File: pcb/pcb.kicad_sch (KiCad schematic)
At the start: 7 parts

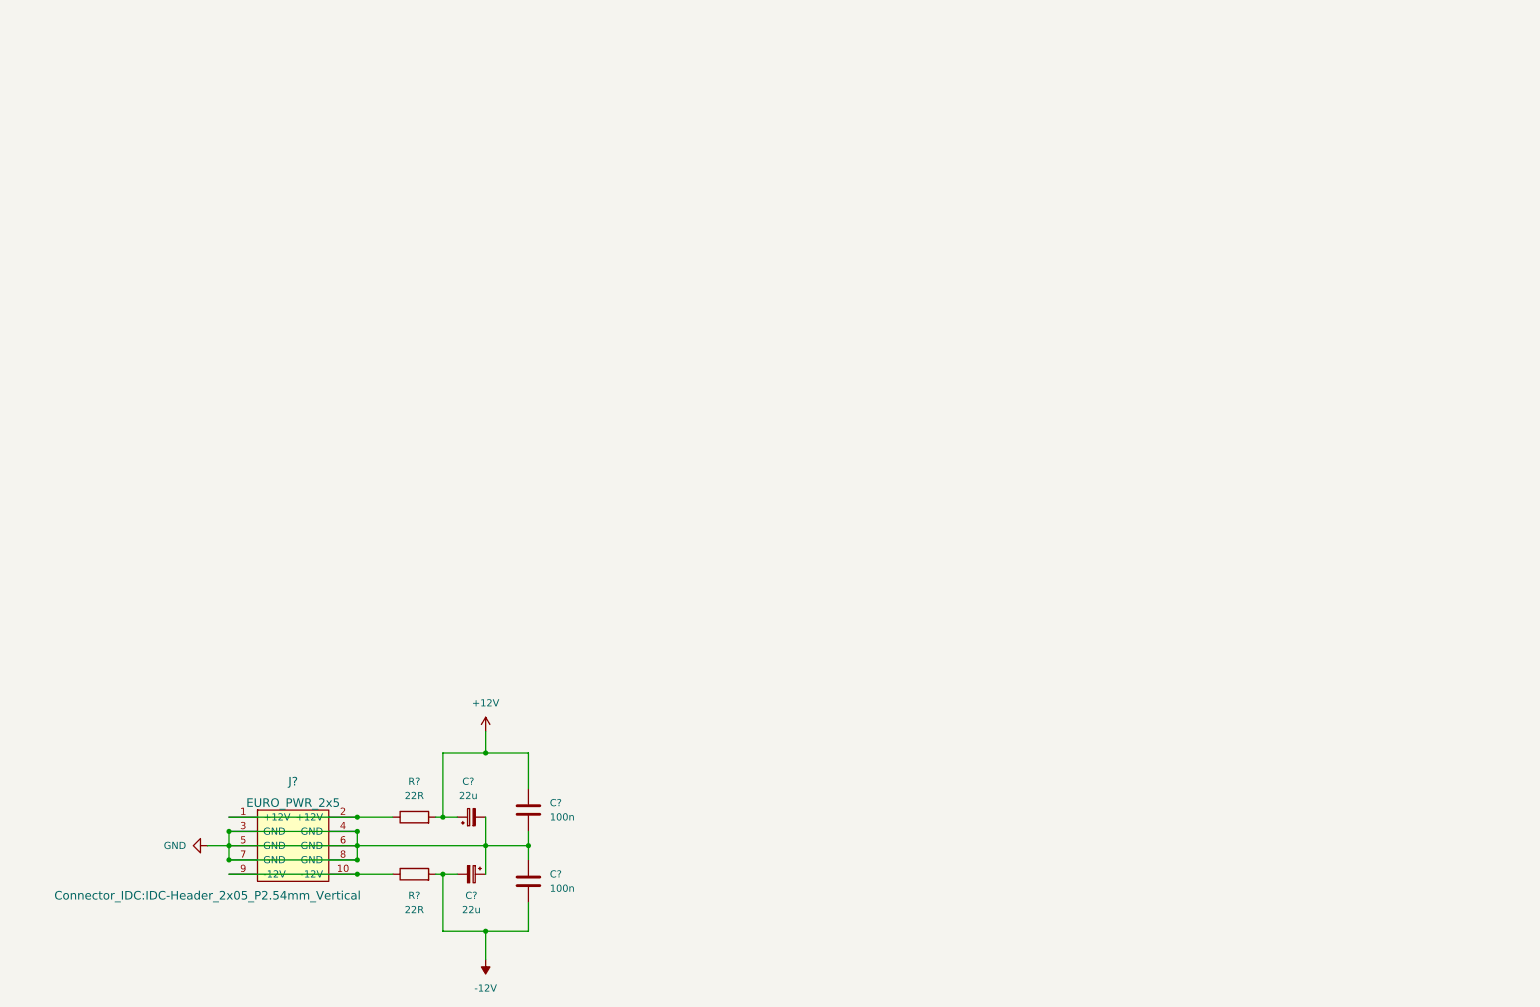
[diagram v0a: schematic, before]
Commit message: Add schematic, first panel design
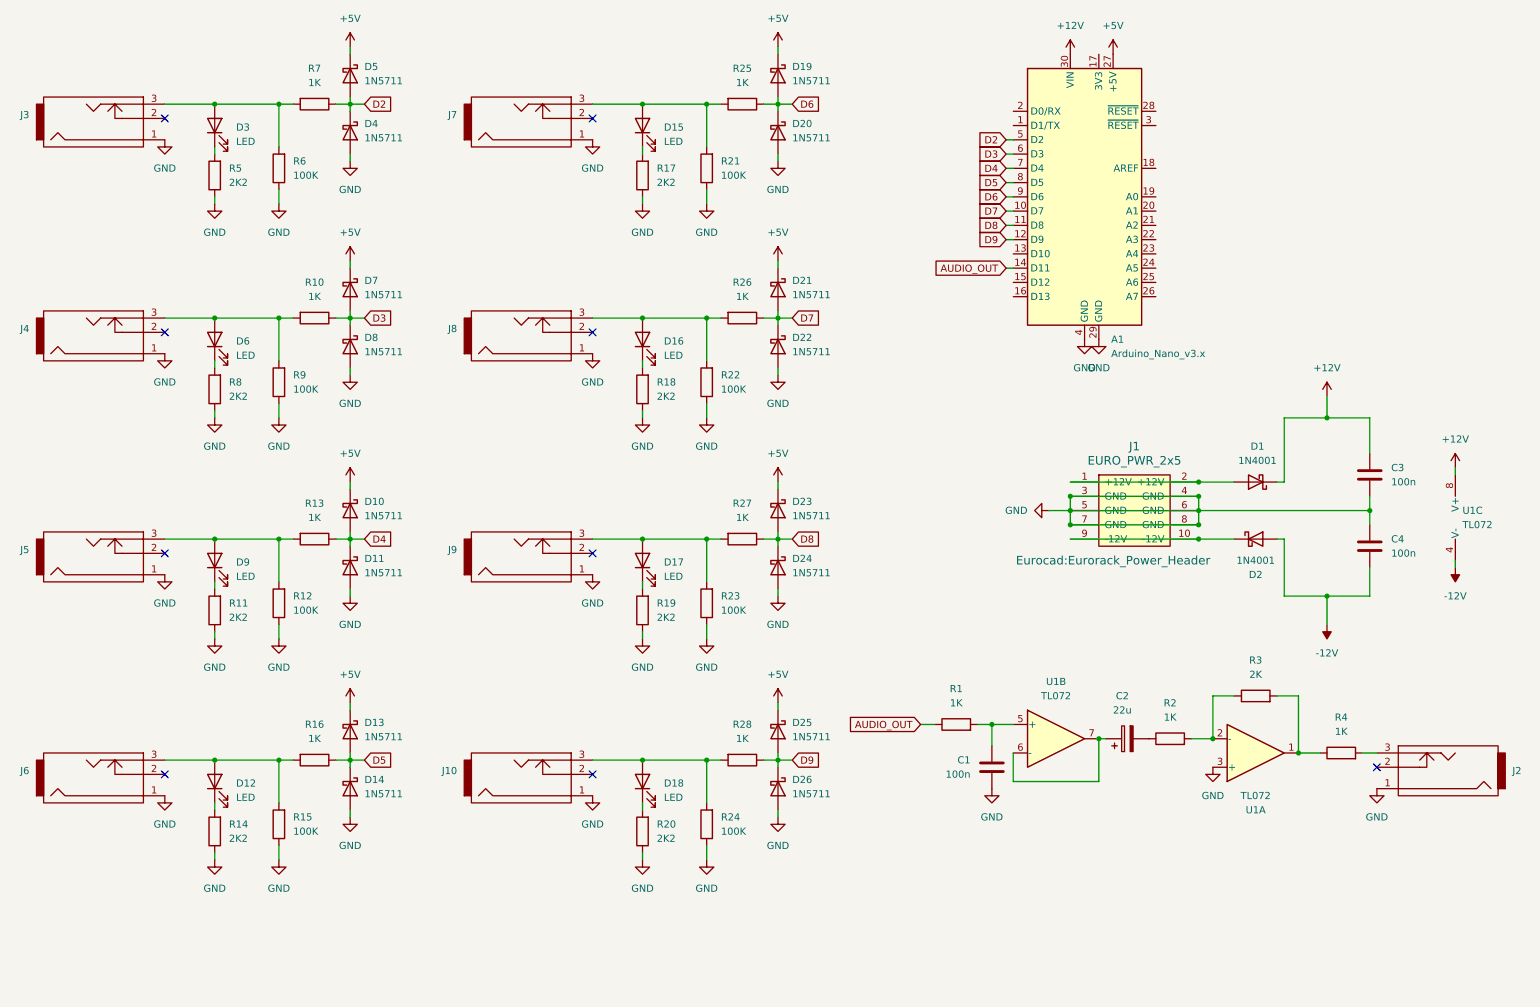
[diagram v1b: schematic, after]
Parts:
- removed C? (x2): 100n, Capacitor_SMD:C_0603_1608Metric, symbol Device:C
- removed C? (x2): 22u, Capacitor_SMD:CP_Elec_4x3.9, symbol Device:C_Polarized_Small
- removed J?: EURO_PWR_2x5, Connector_IDC:IDC-Header_2x05_P2.54mm_Vertical, symbol eurocad:EURO_PWR_2x5
- removed R? (x2): 22R, Resistor_SMD:R_0603_1608Metric, symbol Device:R
- added A1: Arduino_Nano_v3.x, Module:Arduino_Nano, symbol MCU_Module:Arduino_Nano_v3.x
- added C1, C3, C4: 100n, Capacitor_THT:C_Rect_L7.2mm_W3.0mm_P5.00mm_FKS2_FKP2_MKS2_MKP2, symbol Device:C
- added C2: 22u, Capacitor_THT:CP_Radial_D5.0mm_P2.50mm, symbol Device:C_Polarized
- added D1, D2: 1N4001, Diode_THT:D_DO-41_SOD81_P10.16mm_Horizontal, symbol Diode:1N5819
- added D10, D11, D13, D14, D19, D20, D21, D22, D23, D24, D25, D26, D4, D5, D7, D8: 1N5711, Diode_THT:D_DO-41_SOD81_P10.16mm_Horizontal, symbol Diode:1N5819
- added D12, D15, D16, D17, D18, D3, D6, D9: LED, LED_THT:LED_D3.0mm, symbol Device:LED
- added J1: EURO_PWR_2x5, Eurocad:Eurorack_Power_Header, symbol eurocad:EURO_PWR_2x5
- added J10, J2, J3, J4, J5, J6, J7, J8, J9: PJ301M-12, Eurocad:PJ301M-12, symbol eurocad:PJ301M-12
- added R1, R10, R13, R16, R2, R25, R26, R27, R28, R4, R7: 1K, Resistor_THT:R_Axial_DIN0207_L6.3mm_D2.5mm_P7.62mm_Horizontal, symbol Device:R
- added R11, R14, R17, R18, R19, R20, R5, R8: 2K2, Resistor_THT:R_Axial_DIN0207_L6.3mm_D2.5mm_P7.62mm_Horizontal, symbol Device:R
- added R12, R15, R21, R22, R23, R24, R6, R9: 100K, Resistor_THT:R_Axial_DIN0207_L6.3mm_D2.5mm_P7.62mm_Horizontal, symbol Device:R
- added R3: 2K, Resistor_THT:R_Axial_DIN0207_L6.3mm_D2.5mm_P7.62mm_Horizontal, symbol Device:R
- added U1: TL072, symbol Amplifier_Operational:TL072
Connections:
- net +12V: now also A1.30 (VIN), C3.1, D1.1 (K), U1.8 (V+)
- net -12V: now also C4.2, D2.2 (A), U1.4 (V-)
- net GND: now also A1.29 (GND), A1.4 (GND), C1.2, C3.2, C4.1, D11.2 (A), D14.2 (A), D20.2 (A), D22.2 (A), D24.2 (A), D26.2 (A), D4.2 (A), D8.2 (A), J1.3 (GND), J1.4 (GND), J1.5 (GND), J1.6 (GND), J1.7 (GND), J1.8 (GND), J10.1, J2.1, J3.1, J4.1, J5.1, J6.1, J7.1, J8.1, J9.1, R11.1, R12.1, R14.1, R15.1, R17.1, R18.1, R19.1, R20.1, R21.1, R22.1, R23.1, R24.1, R5.1, R6.1, R8.1, R9.1, U1.3 (+)
- new net: D12.2 (A), J6.3, R15.2, R16.2
- new net: D12.1 (K), R14.2
- new net: D18.2 (A), J10.3, R24.2, R28.2
- new net: D16.2 (A), J8.3, R22.2, R26.2
- new net: D6.2 (A), J4.3, R10.2, R9.2
- new net: D18.1 (K), R20.2
- new net: D3.1 (K), R5.2
- new net: D3.2 (A), J3.3, R6.2, R7.2
- new net: D2.1 (K), J1.10 (-12V), J1.9 (-12V)
- new net: R2.2, R3.1, U1.2 (-)
- new net: R3.2, R4.1, U1.1
- new net: C1.1, R1.2, U1.5 (+)
- new net: D9.1 (K), R11.2
- new net: D9.2 (A), J5.3, R12.2, R13.2
- new net: D17.1 (K), R19.2
- new net: D17.2 (A), J9.3, R23.2, R27.2
- new net: C2.1, U1.6 (-), U1.7
- new net: C2.2, R2.1
- new net: D15.2 (A), J7.3, R21.2, R25.2
- new net: D15.1 (K), R17.2
- new net: D6.1 (K), R8.2
- new net: J2.3, R4.2
- new net: D16.1 (K), R18.2
- new net: D1.2 (A), J1.1 (+12V), J1.2 (+12V)
- new net +5V: A1.27 (+5V), D10.1 (K), D13.1 (K), D19.1 (K), D21.1 (K), D23.1 (K), D25.1 (K), D5.1 (K), D7.1 (K)
- new net AUDIO_OUT: A1.14 (D11), R1.1
- new net D2: A1.5 (D2), D4.1 (K), D5.2 (A), R7.1
- new net D3: A1.6 (D3), D7.2 (A), D8.1 (K), R10.1
- new net D4: A1.7 (D4), D10.2 (A), D11.1 (K), R13.1
- new net D5: A1.8 (D5), D13.2 (A), D14.1 (K), R16.1
- new net D6: A1.9 (D6), D19.2 (A), D20.1 (K), R25.1
- new net D7: A1.10 (D7), D21.2 (A), D22.1 (K), R26.1
- new net D8: A1.11 (D8), D23.2 (A), D24.1 (K), R27.1
- new net D9: A1.12 (D9), D25.2 (A), D26.1 (K), R28.1
- no-connect marks 0 -> 9

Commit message: Finish pcb
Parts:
- D10, D11, D13, D14, D19, D20, D21, D22, D23, D24, D25, D26, D4, D5, D7, D8: footprint Diode_THT:D_DO-41_SOD81_P10.16mm_Horizontal -> Diode_THT:D_DO-35_SOD27_P7.62mm_Horizontal
- U1: footprint (none) -> Package_DIP:DIP-8_W7.62mm
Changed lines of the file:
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@@
       (effects (font (size 1.27 1.27)) (justify left))
     )
-    (property "Footprint" "Diode_THT:D_DO-41_SOD81_P10.16mm_Horizontal" (at 145.415 76.2 0)
+    (property "Footprint" "Diode_THT:D_DO-35_SOD27_P7.62mm_Horizontal" (at 145.415 76.2 0)
       (effects (font (size 1.27 1.27)) hide)
     )
@@
       (effects (font (size 1.27 1.27)) (justify left))
     )
-    (property "Footprint" "Diode_THT:D_DO-41_SOD81_P10.16mm_Horizontal" (at 69.215 66.04 0)
+    (property "Footprint" "Diode_THT:D_DO-35_SOD27_P7.62mm_Horizontal" (at 69.215 66.04 0)
       (effects (font (size 1.27 1.27)) hide)
     )
@@
       (effects (font (size 1.27 1.27)) (justify left))
     )
-    (property "Footprint" "Diode_THT:D_DO-41_SOD81_P10.16mm_Horizontal" (at 145.415 66.04 0)
+    (property "Footprint" "Diode_THT:D_DO-35_SOD27_P7.62mm_Horizontal" (at 145.415 66.04 0)
       (effects (font (size 1.27 1.27)) hide)
     )
@@
       (effects (font (size 1.27 1.27)) (justify left))
     )
-    (property "Footprint" "Diode_THT:D_DO-41_SOD81_P10.16mm_Horizontal" (at 69.215 154.94 0)
+    (property "Footprint" "Diode_THT:D_DO-35_SOD27_P7.62mm_Horizontal" (at 69.215 154.94 0)
       (effects (font (size 1.27 1.27)) hide)
     )
@@
       (effects (font (size 1.27 1.27)))
     )
-    (property "Footprint" "" (at 234.95 148.59 0)
+    (property "Footprint" "Package_DIP:DIP-8_W7.62mm" (at 234.95 148.59 0)
       (effects (font (size 1.27 1.27)) hide)
     )
@@
       (effects (font (size 1.27 1.27)) (justify left))
     )
-    (property "Footprint" "Diode_THT:D_DO-41_SOD81_P10.16mm_Horizontal" (at 145.415 144.78 0)
+    (property "Footprint" "Diode_THT:D_DO-35_SOD27_P7.62mm_Horizontal" (at 145.415 144.78 0)
       (effects (font (size 1.27 1.27)) hide)
     )
@@
       (effects (font (size 1.27 1.27)) (justify left))
     )
-    (property "Footprint" "Diode_THT:D_DO-41_SOD81_P10.16mm_Horizontal" (at 69.215 27.94 0)
+    (property "Footprint" "Diode_THT:D_DO-35_SOD27_P7.62mm_Horizontal" (at 69.215 27.94 0)
       (effects (font (size 1.27 1.27)) hide)
     )
@@
       (effects (font (size 1.27 1.27)) (justify left))
     )
-    (property "Footprint" "Diode_THT:D_DO-41_SOD81_P10.16mm_Horizontal" (at 145.415 38.1 0)
+    (property "Footprint" "Diode_THT:D_DO-35_SOD27_P7.62mm_Horizontal" (at 145.415 38.1 0)
       (effects (font (size 1.27 1.27)) hide)
     )
@@
       (effects (font (size 1.27 1.27)) (justify left))
     )
-    (property "Footprint" "Diode_THT:D_DO-41_SOD81_P10.16mm_Horizontal" (at 145.415 27.94 0)
+    (property "Footprint" "Diode_THT:D_DO-35_SOD27_P7.62mm_Horizontal" (at 145.415 27.94 0)
       (effects (font (size 1.27 1.27)) hide)
     )
@@
       (effects (font (size 1.27 1.27)) (justify left))
     )
-    (property "Footprint" "Diode_THT:D_DO-41_SOD81_P10.16mm_Horizontal" (at 69.215 38.1 0)
+    (property "Footprint" "Diode_THT:D_DO-35_SOD27_P7.62mm_Horizontal" (at 69.215 38.1 0)
       (effects (font (size 1.27 1.27)) hide)
     )
@@
       (effects (font (size 1.27 1.27)))
     )
-    (property "Footprint" "" (at 199.39 146.05 0)
+    (property "Footprint" "Package_DIP:DIP-8_W7.62mm" (at 199.39 146.05 0)
       (effects (font (size 1.27 1.27)) hide)
     )
@@
       (effects (font (size 1.27 1.27)) (justify left))
     )
-    (property "Footprint" "Diode_THT:D_DO-41_SOD81_P10.16mm_Horizontal" (at 69.215 115.57 0)
+    (property "Footprint" "Diode_THT:D_DO-35_SOD27_P7.62mm_Horizontal" (at 69.215 115.57 0)
       (effects (font (size 1.27 1.27)) hide)
     )
@@
       (effects (font (size 1.27 1.27)) (justify left))
     )
-    (property "Footprint" "Diode_THT:D_DO-41_SOD81_P10.16mm_Horizontal" (at 145.415 105.41 0)
+    (property "Footprint" "Diode_THT:D_DO-35_SOD27_P7.62mm_Horizontal" (at 145.415 105.41 0)
       (effects (font (size 1.27 1.27)) hide)
     )
@@
       (effects (font (size 1.27 1.27)) (justify left))
     )
-    (property "Footprint" "Diode_THT:D_DO-41_SOD81_P10.16mm_Horizontal" (at 145.415 154.94 0)
+    (property "Footprint" "Diode_THT:D_DO-35_SOD27_P7.62mm_Horizontal" (at 145.415 154.94 0)
       (effects (font (size 1.27 1.27)) hide)
     )
@@
       (effects (font (size 1.27 1.27)) (justify left))
     )
-    (property "Footprint" "Diode_THT:D_DO-41_SOD81_P10.16mm_Horizontal" (at 145.415 115.57 0)
+    (property "Footprint" "Diode_THT:D_DO-35_SOD27_P7.62mm_Horizontal" (at 145.415 115.57 0)
       (effects (font (size 1.27 1.27)) hide)
     )
@@
       (effects (font (size 1.27 1.27)) (justify left))
     )
-    (property "Footprint" "Diode_THT:D_DO-41_SOD81_P10.16mm_Horizontal" (at 69.215 105.41 0)
+    (property "Footprint" "Diode_THT:D_DO-35_SOD27_P7.62mm_Horizontal" (at 69.215 105.41 0)
       (effects (font (size 1.27 1.27)) hide)
     )
@@
       (effects (font (size 1.27 1.27)) (justify left))
     )
-    (property "Footprint" "" (at 273.05 106.68 0)
+    (property "Footprint" "Package_DIP:DIP-8_W7.62mm" (at 273.05 106.68 0)
       (effects (font (size 1.27 1.27)) hide)
     )
@@
       (effects (font (size 1.27 1.27)) (justify left))
     )
-    (property "Footprint" "Diode_THT:D_DO-41_SOD81_P10.16mm_Horizontal" (at 69.215 144.78 0)
+    (property "Footprint" "Diode_THT:D_DO-35_SOD27_P7.62mm_Horizontal" (at 69.215 144.78 0)
       (effects (font (size 1.27 1.27)) hide)
     )
@@
       (effects (font (size 1.27 1.27)) (justify left))
     )
-    (property "Footprint" "Diode_THT:D_DO-41_SOD81_P10.16mm_Horizontal" (at 69.215 76.2 0)
-      (effects (font (size 1.27 1.27)) hide)
-    )
+    (property "Footprint" "Diode_THT:D_DO-35_SOD27_P7.62mm_Horizontal" (at 69.215 76.2 0)
+      (effects (font (size 1.27 1.27)) hide)
+    )
